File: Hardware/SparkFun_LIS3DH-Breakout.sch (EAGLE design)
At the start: 18 parts, among them U2 LIS3DH

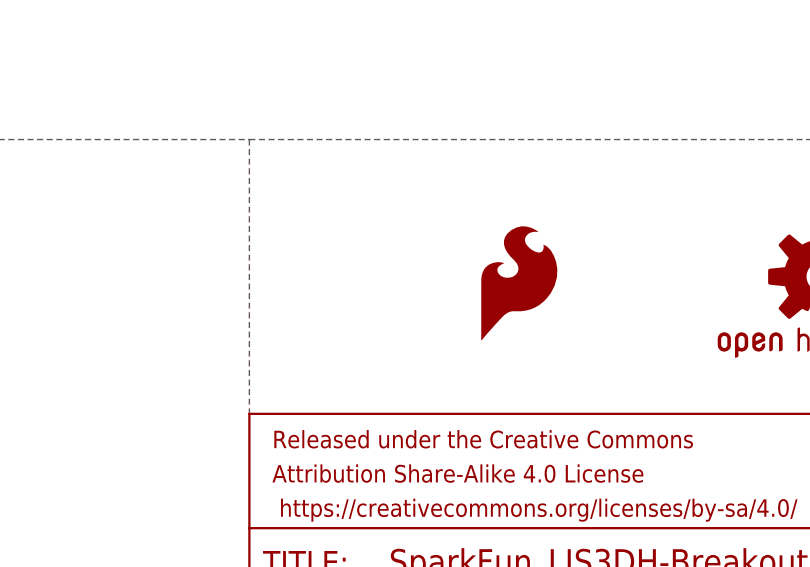
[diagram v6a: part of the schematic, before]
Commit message: removed 'ADR' and : silks
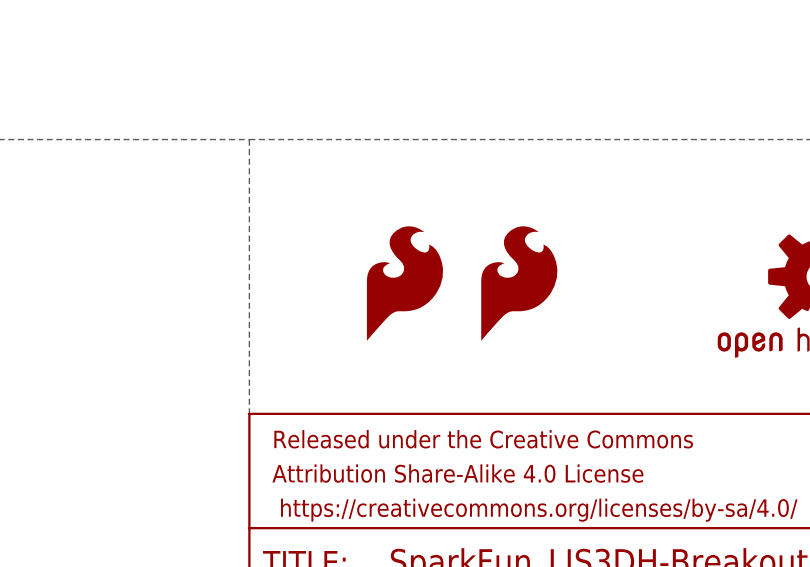
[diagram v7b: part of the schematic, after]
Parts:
- added LOGO2: SFE_LOGO_FLAME.1_INCH, SparkFun-Aesthetics:SFE_LOGO_FLAME.1_INCH
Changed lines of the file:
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@@
 <part name="J2" library="SparkFun-Connectors" deviceset="CONN_06" device="NO_SILK_FEMALE_PTH"/>
 <part name="GND4" library="SparkFun" deviceset="GND" device=""/>
+<part name="LOGO2" library="SparkFun-Aesthetics" deviceset="SFE_LOGO_FLAME" device=".1_INCH"/>
 </parts>
 <sheets>
@@
 <instance part="J2" gate="G$1" x="99.06" y="27.94" rot="R180"/>
 <instance part="GND4" gate="1" x="76.2" y="27.94"/>
+<instance part="LOGO2" gate="G$1" x="160.02" y="43.18"/>
 </instances>
 <busses>

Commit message: Applied review changes
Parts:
- renumbered U2 to U1
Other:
- note added: "Address selection jumper SJ1"
- note added: "Closed: 0x18 (SA0 = 0) Open: 0x19 (SA0 = 1)"
- note added: "MODES: I2C: Leave the copper-connected jumper SJ2 as default, use SJ1 to set the I2C address between 0x18 and 0x19. SJ1 is the LSB of the address. SPI 4-WIRE: Jumpers SJ2 can be opened to remove 4.7k load on the SPI lines. SJ1 must be open for SPI operation."
- note removed: "I2C Address:"
- note removed: "Jumper open by default, so SA0 = 1"
- note removed: "MODES: I2C: Leave the copper-connected jumper SJ2 as default, use SJ1 to set the I2C address between 0x18 and 0x19. SJ1 is the LSB of the address. SPI 4-WIRE: Jumpers SJ2 can be opened to remove 4.7k load on the SPI lines. Open SJ1"
- note removed: "SA0 = 0: 0x18"
- note removed: "SA0 = 1: 0x19"
- moved on the sheet: J1, J2
